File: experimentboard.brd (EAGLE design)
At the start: 105.4 x 100 mm, 72 parts, among them IC1 TL072P, IC2 LM317, IC3 LM337, Q1 27 MHz, U1 PCM1690, U2 PLL1706

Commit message: Taking the Beaglebone approach
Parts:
- removed C16, C17, C18: 100 nF ml, rcl:C050-024X044
- removed Q1: 27 MHz, special:QS
- removed R2: 22, rcl:0207/7
- removed SV1: (no value), 0000halfgaar:MA20-2
- added JP1, JP2: (no value), jumper:JP2Q
- added R15: 680, rcl:0207/7
- added R27: 0, rcl:0207/10
- added R30, R31, R32, R33, R35, R36, R37: 22, rcl:0207/7
- added R38, R39: 5.6k, rcl:0207/7
- added U$2: BEAGLEBONEP9, 0000halfgaar:HEADERS23-2
- C1: value 22pf -> 4.7n
- C15: value 100 nF ml -> 1µF ml
- C2: value 22pf -> 68n
- R1: value 22 -> 0; device rcl:0207/7 -> rcl:0207/10
- R23, R24: value 2.7k -> 715
- R3: value 22 -> 10k
- U2: value PLL1706 -> DIR9001; device 0000halfgaar:SSOP20 -> 0000halfgaar:TSSOP28
- moved AOUT 136.2 mm to (135.9, 64.8)
- moved AC 118.9 mm to (16.5, 105.4), turned to 0 degrees
- moved D3 112.7 mm to (8.89, 97.8), turned to 0 degrees
- moved D4 95.0 mm to (33.0, 97.8), turned to 0 degrees
- moved C24 94.5 mm to (8.89, 86.4), turned to 0 degrees
- moved D6 80.8 mm to (5.08, 71.1), turned to 90 degrees
- moved R1 80.2 mm to (39.4, 11.4)
- moved D7 74.8 mm to (11.4, 74.9), turned to 0 degrees
- moved C5 74.5 mm to (93.2, 70.2), turned to 90 degrees
- moved C15 73.0 mm to (14.0, 3.81), turned to 0 degrees
- moved C25 72.5 mm to (33.0, 86.4), turned to 0 degrees
- moved C28 70.3 mm to (6.35, 61.0), turned to 270 degrees
- moved C26 70.1 mm to (11.4, 71.1), turned to 0 degrees
- moved U2 68.1 mm to (108.0, 69.8), flipped to the top, turned to 180 degrees
- moved IC2 63.6 mm to (11.4, 64.8), turned to 180 degrees
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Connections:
- removed net MOSI: SV1.19, U1.20, U2.5
- removed net N$10: R1.1, SV1.35
- removed net N$9: R2.1, SV1.12
- removed net SCKL: SV1.23, U1.21, U2.6
- removed net U1SEL: SV1.15, U1.22
- removed net U2SEL: SV1.10, U2.7
- new net ACLKR: R31.1, U$2.12
- new net ACLKX: R36.1, U$2.31
- new net AHCLKX: R35.1, U$2.29
- new net DIN: R32.1, U$2.32
- new net DIR_AUDIO: U$2.16, U2.1
- new net DOUT: R37.1, U$2.28
- new net FSR: R30.1, U$2.27
- new net MCLK: R4.1, U$2.25
- new net N$20: U2.20
- new net N$51: R32.2, U2.12
- new net N$52: R31.2, U2.11
- new net N$53: R30.2, U2.10
- new net N$54: R33.2, U2.4
- new net N$61: R37.2, U1.8
- new net N$62: R36.2, U1.7
- new net N$63: R35.2, U1.6
- new net RST: U$2.15, U1.15, U2.21
- new net SCL: R38.1, U$2.17, U1.21
- new net SDA: R39.1, U$2.18, U1.20
- net AGND: now also C1.1, C2.1, R1.2, U2.23; no longer C16.1, U2.9
- net DGND: now also C15.2, R1.1, R7.1, U$2.1, U$2.2, U2.19, U2.6, U2.8; no longer C1.1, C15.1, C17.1, C18.2, C2.1, SV1.9, U2.16, U2.17, U2.4
- net N$1: now also JP2.3, U2.14; no longer R1.2, U1.6
- net N$2: now also R3.2, U1.23; no longer R2.2, U1.7
- net N$3: now also JP2.1, U2.13; no longer R3.2, U1.8
- net N$4: now also C1.2, R15.1, U2.22; no longer R4.1, U2.3
- net N$6: now also C2.2, R15.2; no longer C1.2, Q1.2, U2.10
- net N$7: now also JP1.4, U2.25; no longer C2.2, Q1.1, U2.11
- net N$8: now also JP1.2, U2.26; no longer R3.1, SV1.40
- net V+: now also R27.2
- net VCC: now also R27.1, U$2.5, U$2.6, U2.24; no longer C16.2, U2.8
- net VDD: now also C15.1, JP1.1, JP1.3, JP2.2, JP2.4, R3.1, R38.2, R39.2, U$2.3, U$2.4, U2.5; no longer C15.2, C17.2, C18.1, R7.1, SV1.1, SV1.17, U1.15, U2.1, U2.13, U2.20
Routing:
- net VDD: track 78.0 -> 12.0 mm
- net SCKL: track 38.3 -> 0.00 mm
- net MOSI: track 30.0 -> 0.00 mm
- net U2SEL: track 27.1 -> 0.00 mm
- net U1SEL: track 20.3 -> 0.00 mm
- net N$8: track 16.1 -> 0.00 mm
- net N$6: track 14.4 -> 0.00 mm
- net N$9: track 14.3 -> 0.00 mm
- net N$7: track 14.1 -> 0.00 mm
- net N$41: track 17.8 -> 31.0 mm
- net N$36: track 13.0 -> 0.13 mm
- net N$10: track 11.1 -> 0.00 mm
- net DGND: track 9.80 -> 0.00 mm
- net N$35: track 8.51 -> 0.09 mm
- net N$1: track 8.23 -> 0.00 mm
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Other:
- board size 105.4 x 100 mm -> 152.4 x 100 mm

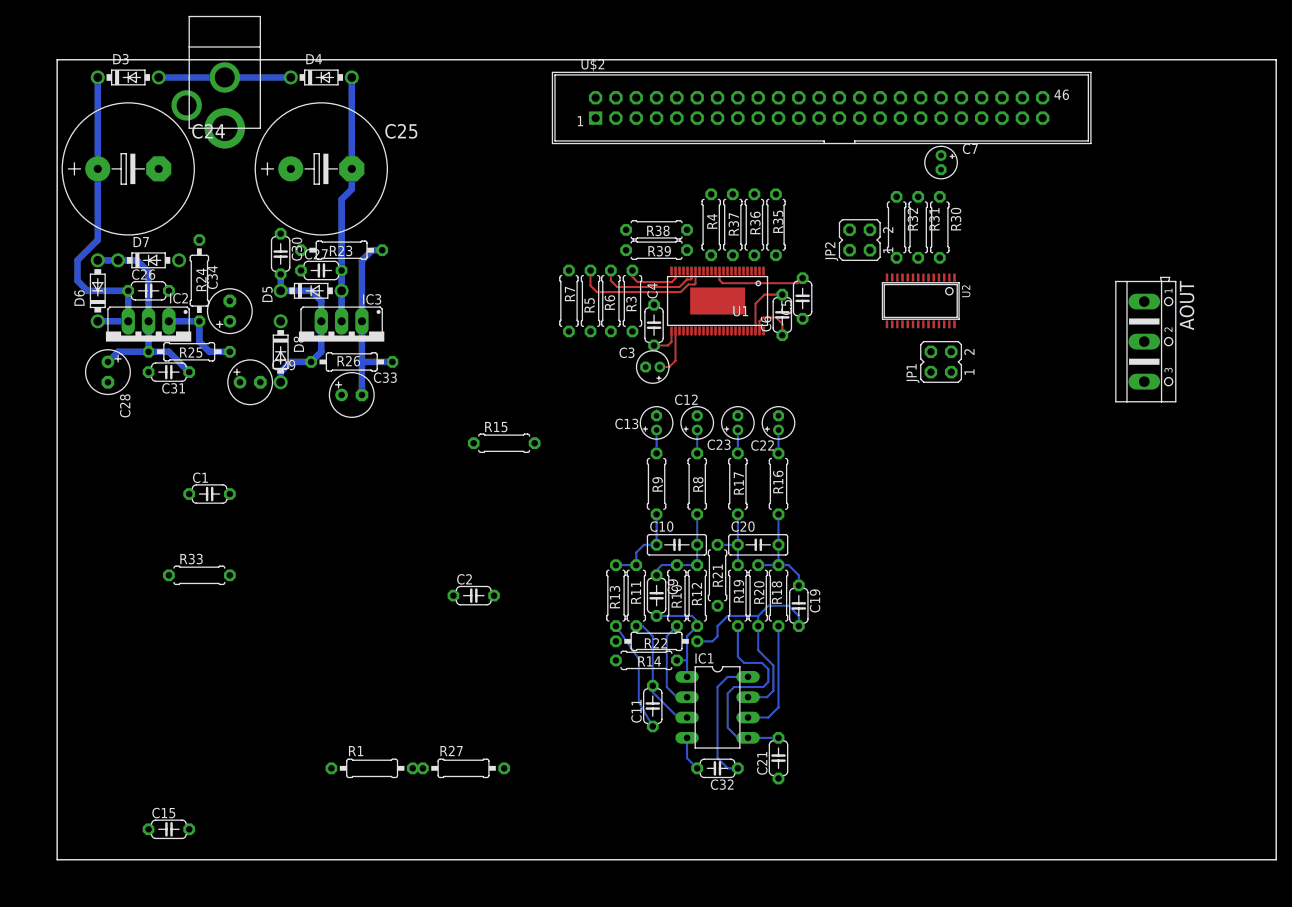
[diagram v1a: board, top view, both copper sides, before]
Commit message: Reversed opamp
Because signals are now on top layer, the layout had to be mirrored.
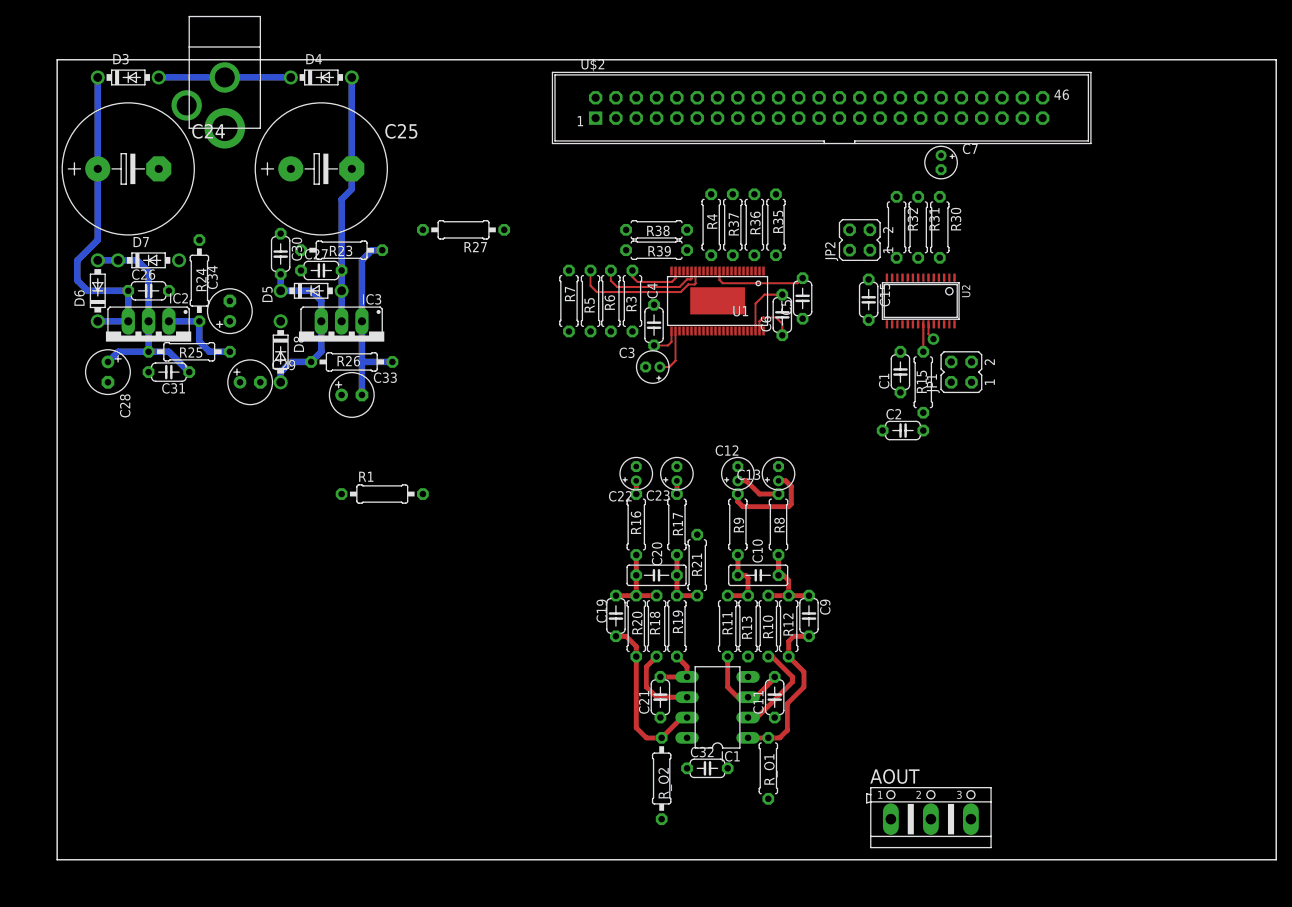
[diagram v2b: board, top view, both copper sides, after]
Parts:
- removed R14: 47, rcl:0207/7
- removed R22: 47, rcl:0207/10
- removed R33: 22, rcl:0207/7
- added R_O1: 47, rcl:0207/7
- added R_O2: 47, rcl:0207/10
- moved C15 109.7 mm to (101.4, 70.0), turned to 270 degrees
- moved C1 87.7 mm to (105.4, 61.0), turned to 90 degrees
- moved R27 67.3 mm to (50.8, 78.7), turned to 180 degrees
- moved AOUT 65.4 mm to (109.2, 5.08), turned to 0 degrees
- moved C2 57.5 mm to (105.7, 53.7)
- moved R15 52.9 mm to (108.3, 59.7), turned to 270 degrees
- moved R1 34.3 mm to (40.6, 45.7)
- moved C19 22.9 mm to (69.8, 30.5)
- moved C9 19.2 mm to (94.0, 30.5)
- moved C22 18.9 mm to (72.4, 48.3)
- moved R16 18.5 mm to (72.4, 41.9)
- moved R13 16.9 mm to (86.4, 29.2)
- moved C21 16.6 mm to (75.4, 20.3)
- moved C13 16.5 mm to (90.2, 48.3)
- moved R18 15.7 mm to (74.9, 29.2)
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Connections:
- net N$26: now also R_O1.1; no longer R14.1
- net N$31: now also R_O2.1; no longer R22.1
- net N$37: now also R_O1.2; no longer R14.2
- net N$38: now also R_O2.2; no longer R22.2
- net N$54: no longer R33.2
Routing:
- net N$30: track 26.7 -> 6.40 mm
- net V+: track 45.0 -> 28.7 mm
- net AGND: track 21.1 -> 9.33 mm, vias 0 -> 1
- net N$31: track 30.7 -> 21.2 mm
- net N$25: track 2.92 -> 12.1 mm
- net N$26: track 14.1 -> 20.9 mm
- net N$32: track 14.5 -> 9.94 mm
- net V-: track 25.8 -> 21.4 mm
- net N$24: track 15.2 -> 11.4 mm
- net N$4: track 0.00 -> 3.44 mm
- net N$15: track 13.2 -> 10.2 mm
- net N$27: track 2.92 -> 5.76 mm
- net N$13: track 10.9 -> 8.70 mm
- net N$18: track 12.3 -> 11.1 mm
- net N$14: track 8.89 -> 7.62 mm
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
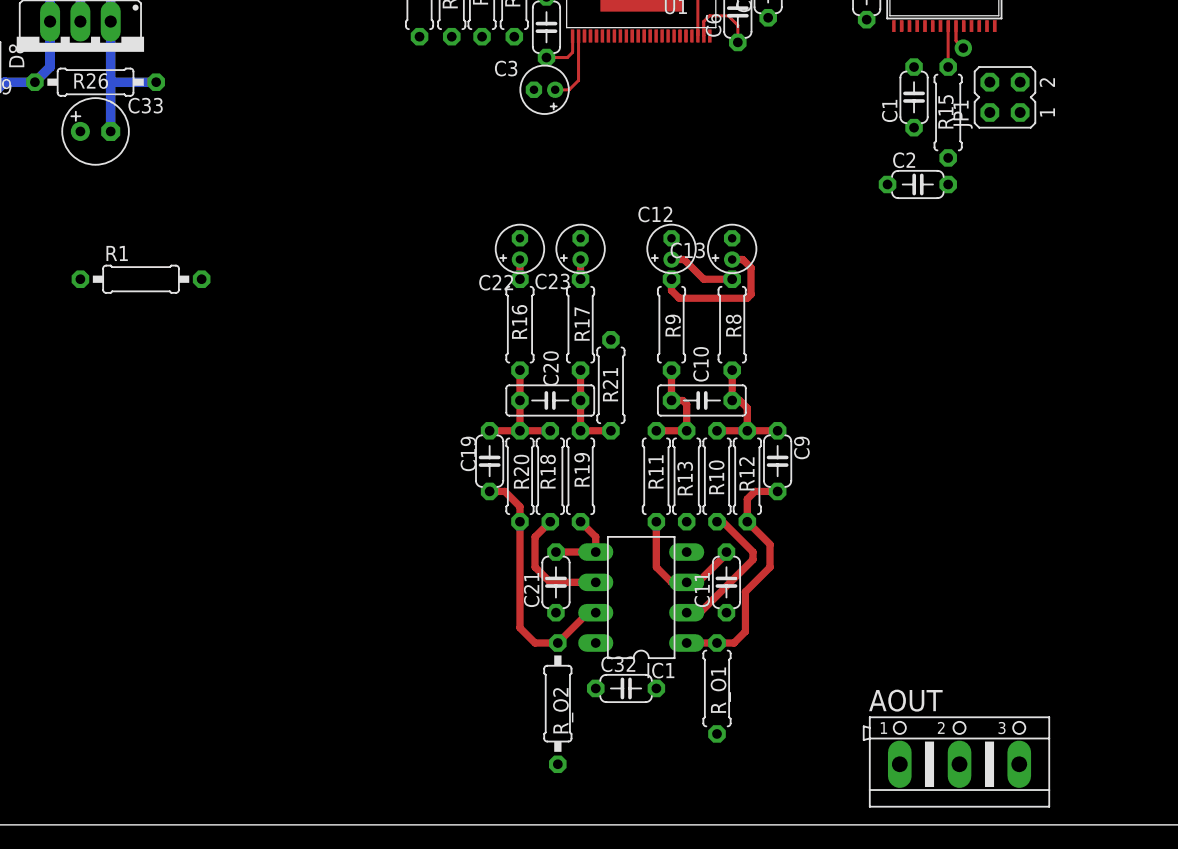
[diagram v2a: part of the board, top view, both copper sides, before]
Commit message: Copied two extra output stages
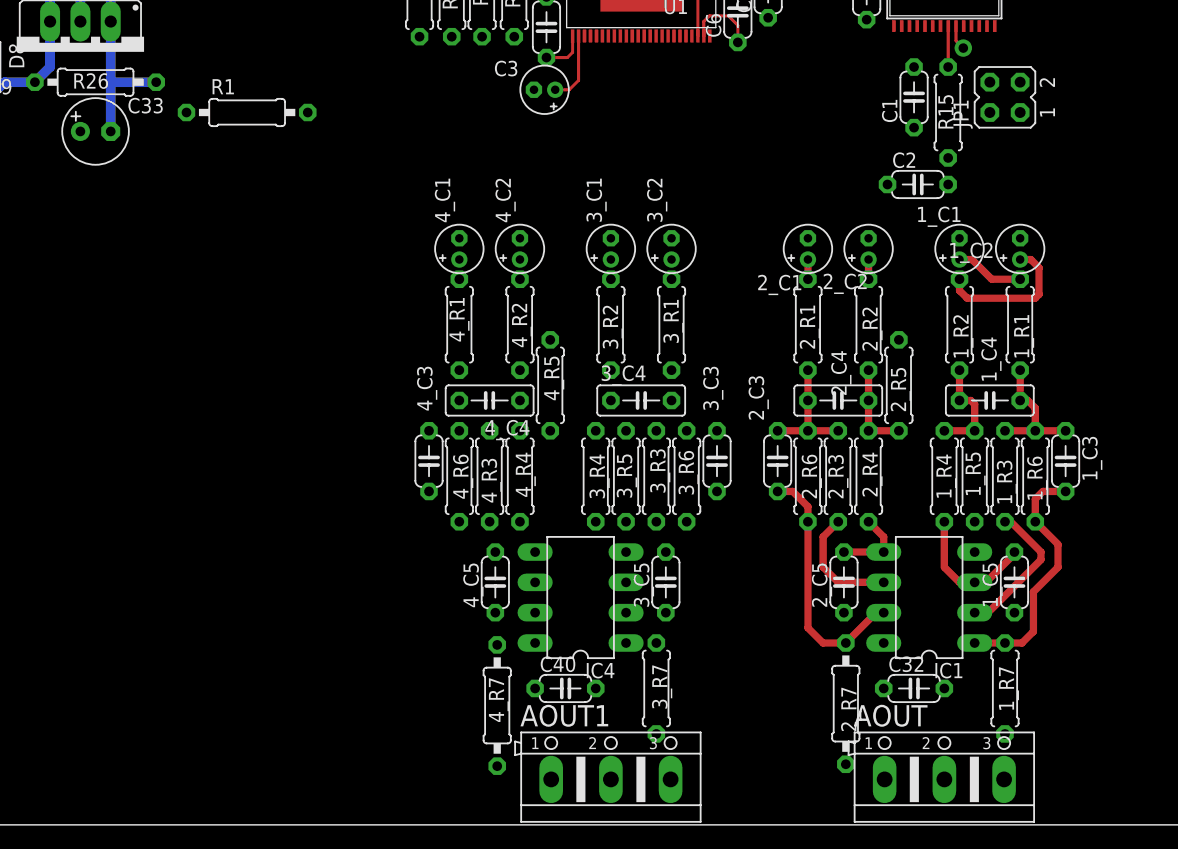
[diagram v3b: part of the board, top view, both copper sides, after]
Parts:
- removed C10, C20: 3.3nF, rcl:C050-025X075
- removed C11, C19, C21: 680pF, rcl:C050-024X044
- removed C13, C23: 10 µF, rcl:E1,8-4
- removed R10, R18, R19: 360, rcl:0207/7
- removed R12, R21: 5.6k, rcl:0207/7
- removed R17, R8: 7.5k, rcl:0207/7
- removed R_O1: 47, rcl:0207/7
- removed R_O2: 47, rcl:0207/10
- added 1_C1, 1_C2, 2_C1, 2_C2, 3_C1, 4_C1: 10 µF, rcl:E1,8-4
- added 1_C3, 1_C5, 2_C5, 3_C3, 3_C5, 4_C3, 4_C5: 680pF, rcl:C050-024X044
- added 1_C4, 2_C4, 3_C4, 4_C4: 3.3nF, rcl:C050-025X075
- added 1_R1, 1_R2, 2_R1, 2_R2, 3_R2, 4_R1: 7.5k, rcl:0207/7
- added 1_R3, 1_R4, 2_R3, 2_R4, 3_R4, 4_R3: 360, rcl:0207/7
- added 1_R5, 1_R6, 2_R5, 2_R6, 3_R5, 4_R5, 4_R6: 5.6k, rcl:0207/7
- added 1_R7, 3_R7: 47, rcl:0207/7
- added 2_R7, 4_R7: 47, rcl:0207/10
- added AOUT1: (no value), con-ptr500:AK500/3
- added C40: 100nf, rcl:C050-024X044
- added IC4: TL072P, 0000halfgaar:DIL8
- 4_R4: value 5.6k -> 360
- moved IC1 24.1 mm to (106.7, 19.1)
- moved C32 24.1 mm to (105.4, 11.4)
- moved R1 16.6 mm to (49.5, 59.7)
- moved AOUT 1.80 mm to (108.0, 3.81)
- turned 3_R6 to 270 degrees
- renumbered C12 to 3_C2, C22 to 4_C2, C9 to 2_C3, R11 to 3_R3, R13 to 3_R6, R16 to 4_R2, R20 to 4_R4, R9 to 3_R1
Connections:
- new net N$10: 3_C3.1, 3_C4.2, 3_R1.2, 3_R3.1, 3_R6.1
- new net N$16: 3_C5.2, 3_R4.2, IC4.3
- new net N$21: 3_C3.2, 3_R6.2, 3_R7.1, IC4.1
- new net N$22: 3_R3.2, IC4.2
- new net N$34: 2_C1.+, 2_R1.1
- new net N$44: 3_C2.+, 3_R2.1
- new net N$45: 3_C1.+, 3_R1.1
- new net N$46: 3_C1.-, U1.39
- new net N$47: 3_C2.-, U1.40
- new net N$48: 4_C4.1, 4_R2.2, 4_R4.1, 4_R5.2
- new net N$49: 4_C3.1, 4_C4.2, 4_R1.2, 4_R3.1, 4_R6.1
- new net N$50: 4_C5.2, 4_R4.2, IC4.5
- new net N$55: 4_C3.2, 4_R6.2, 4_R7.1, IC4.7
- new net N$56: 4_R3.2, IC4.6
- new net N$58: 4_C1.+, 4_R1.1
- new net N$59: 4_C2.-, U1.38
- new net N$60: 4_C1.-, U1.37
- new net N$64: 3_R7.2, AOUT1.3
- new net N$65: 4_R7.2, AOUT1.1
- new net N$9: 3_C4.1, 3_R2.2, 3_R4.1, 3_R5.2
- net AGND: now also 1_C5.1, 1_R5.1, 2_C5.1, 2_R5.1, 3_C5.1, 3_R5.1, 4_C5.1, 4_R5.1, AOUT1.2; no longer 3_R6.1, C11.1, C21.1, R21.1
- net N$13: now also 1_C4.1, 1_R2.2, 1_R4.1, 1_R5.2; no longer 3_R1.2, 3_R3.1, 3_R6.2, C10.1
- net N$14: now also 2_C4.1, 2_R2.2, 2_R4.1, 2_R5.2; no longer C20.1, R17.2, R19.1, R21.2
- net N$15: now also 2_C3.1, 2_C4.2, 2_R1.2, 2_R3.1, 2_R6.1; no longer 4_R2.2, 4_R4.1, C19.1, C20.2, R18.1
- net N$18: now also 1_C3.1, 1_C4.2, 1_R1.2, 1_R3.1, 1_R6.1; no longer 2_C3.1, C10.2, R10.1, R12.1, R8.2
- net N$23: now also 1_R3.2; no longer R10.2
- net N$24: now also 1_C5.2, 1_R4.2; no longer 3_R3.2, C11.2
- net N$25: now also 1_C2.+, 1_R2.1; no longer 3_R1.1, C13.+
- net N$26: now also 1_C3.2, 1_R6.2, 1_R7.1; no longer 2_C3.2, R12.2, R_O1.1
- net N$27: now also 1_C1.+, 1_R1.1; no longer 3_C2.+, R8.1
- net N$28: now also 1_C1.-; no longer 3_C2.-
- net N$29: now also 1_C2.-; no longer C13.-
- net N$30: now also 2_C5.2, 2_R4.2; no longer C21.2, R19.2
- net N$31: now also 2_C3.2, 2_R6.2, 2_R7.1; no longer 4_R4.2, C19.2, R_O2.1
- net N$32: now also 2_R3.2; no longer R18.2
- net N$33: now also 2_C2.+, 2_R2.1; no longer C23.+, R17.1
- net N$35: now also 2_C2.-; no longer C23.-
- net N$36: now also 2_C1.-; no longer 4_C2.-
- net N$37: now also 1_R7.2; no longer R_O1.2
- net N$38: now also 2_R7.2; no longer R_O2.2
- net V+: now also C40.1, IC4.8
- net V-: now also C40.2, IC4.4
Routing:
- net N$57: track 1.65 -> 0.00 mm
- net N$34: track 0.00 -> 1.65 mm
